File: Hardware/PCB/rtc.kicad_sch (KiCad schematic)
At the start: 4 parts, among them U7 DS3232M

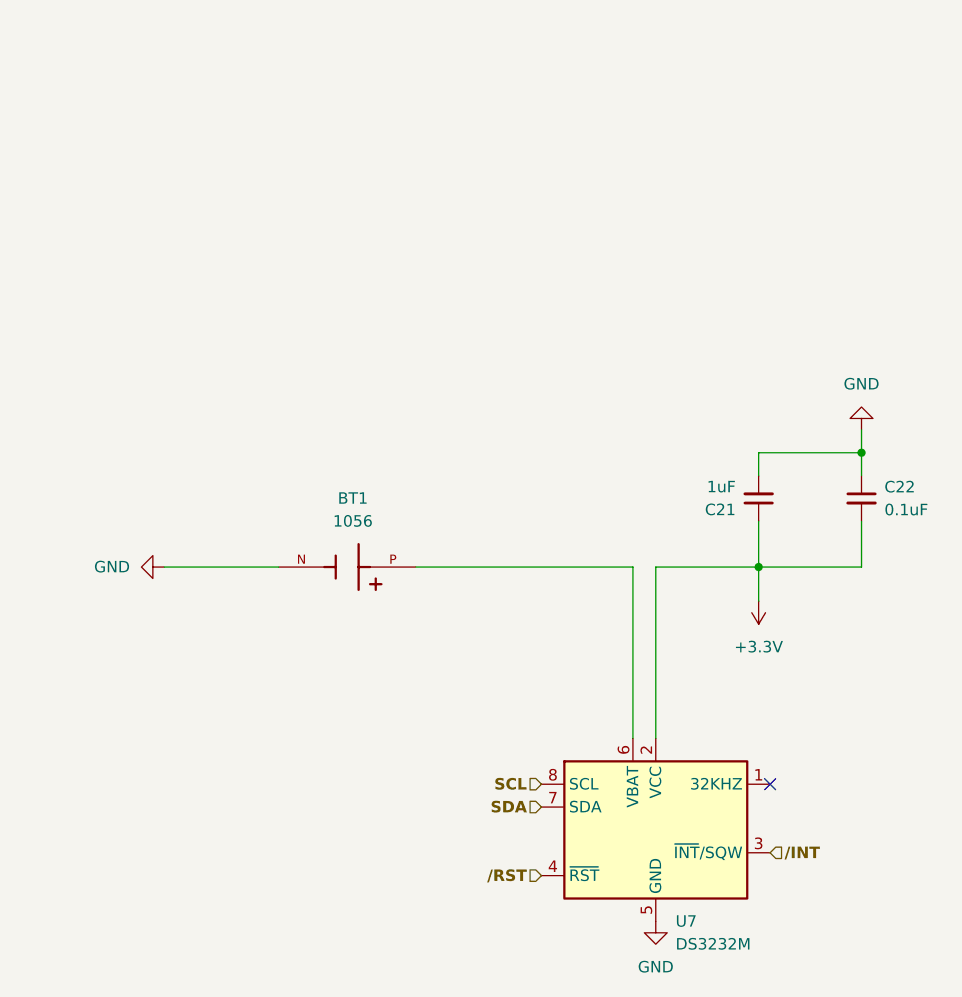
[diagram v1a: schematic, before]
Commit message: Added brushless DC support, fixed terminal blocks too
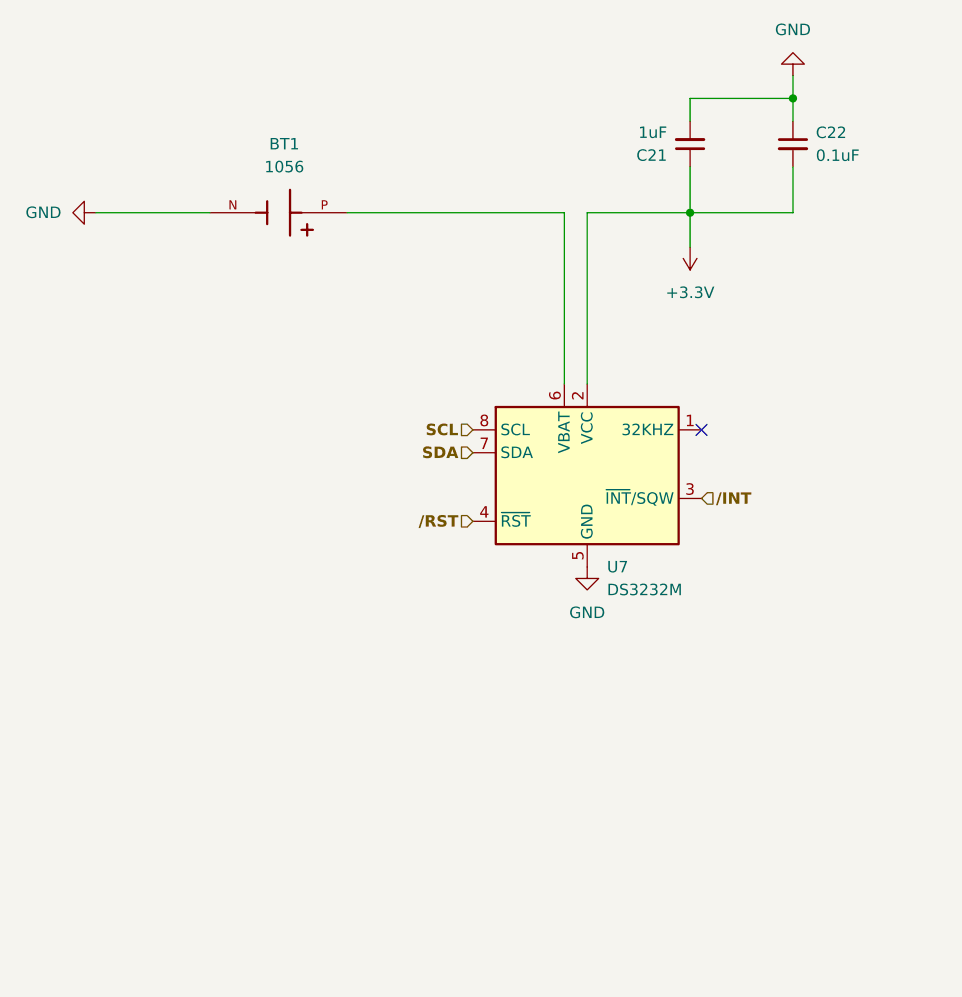
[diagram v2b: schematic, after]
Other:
- moved on the sheet: BT1, C21, C22, U7
